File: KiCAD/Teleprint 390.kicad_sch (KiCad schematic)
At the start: 0 parts

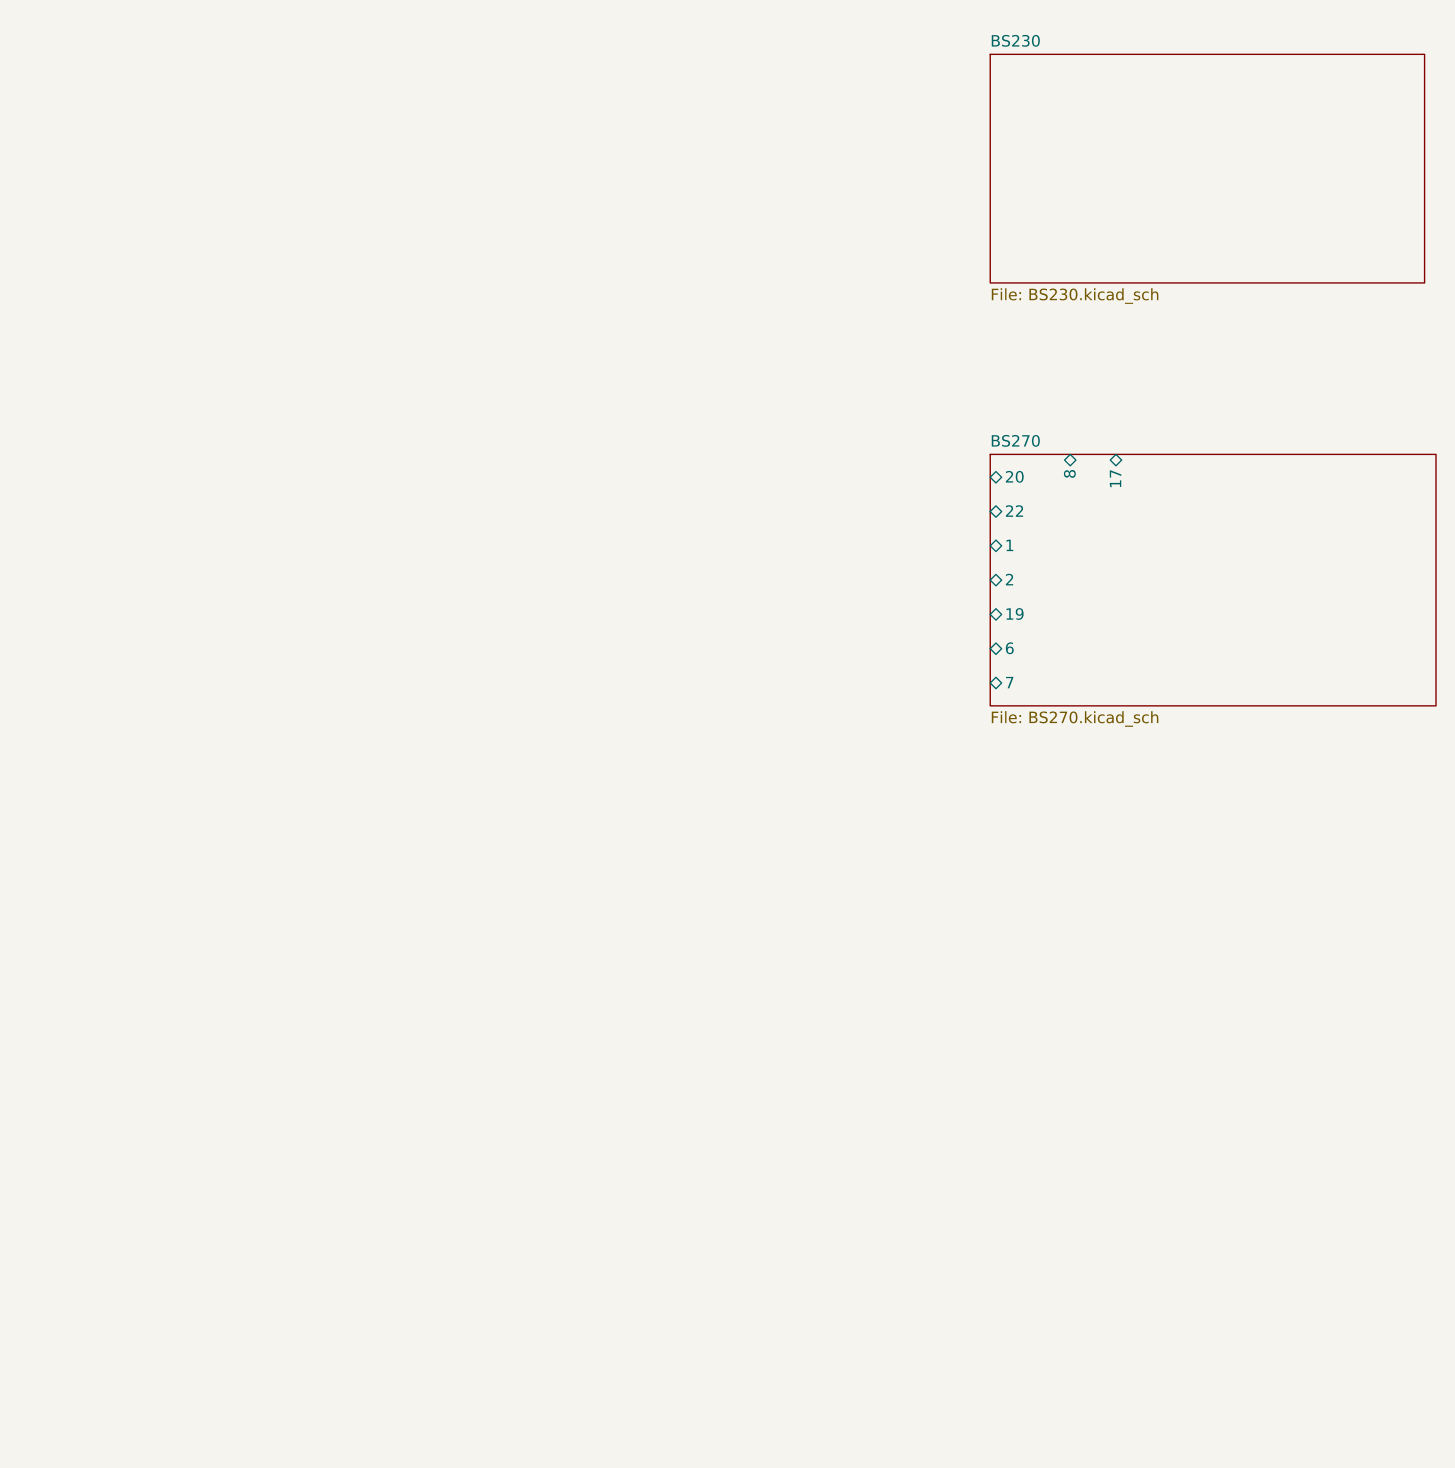
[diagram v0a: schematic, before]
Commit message: Schematics for BS112, BS230 and BS263 added
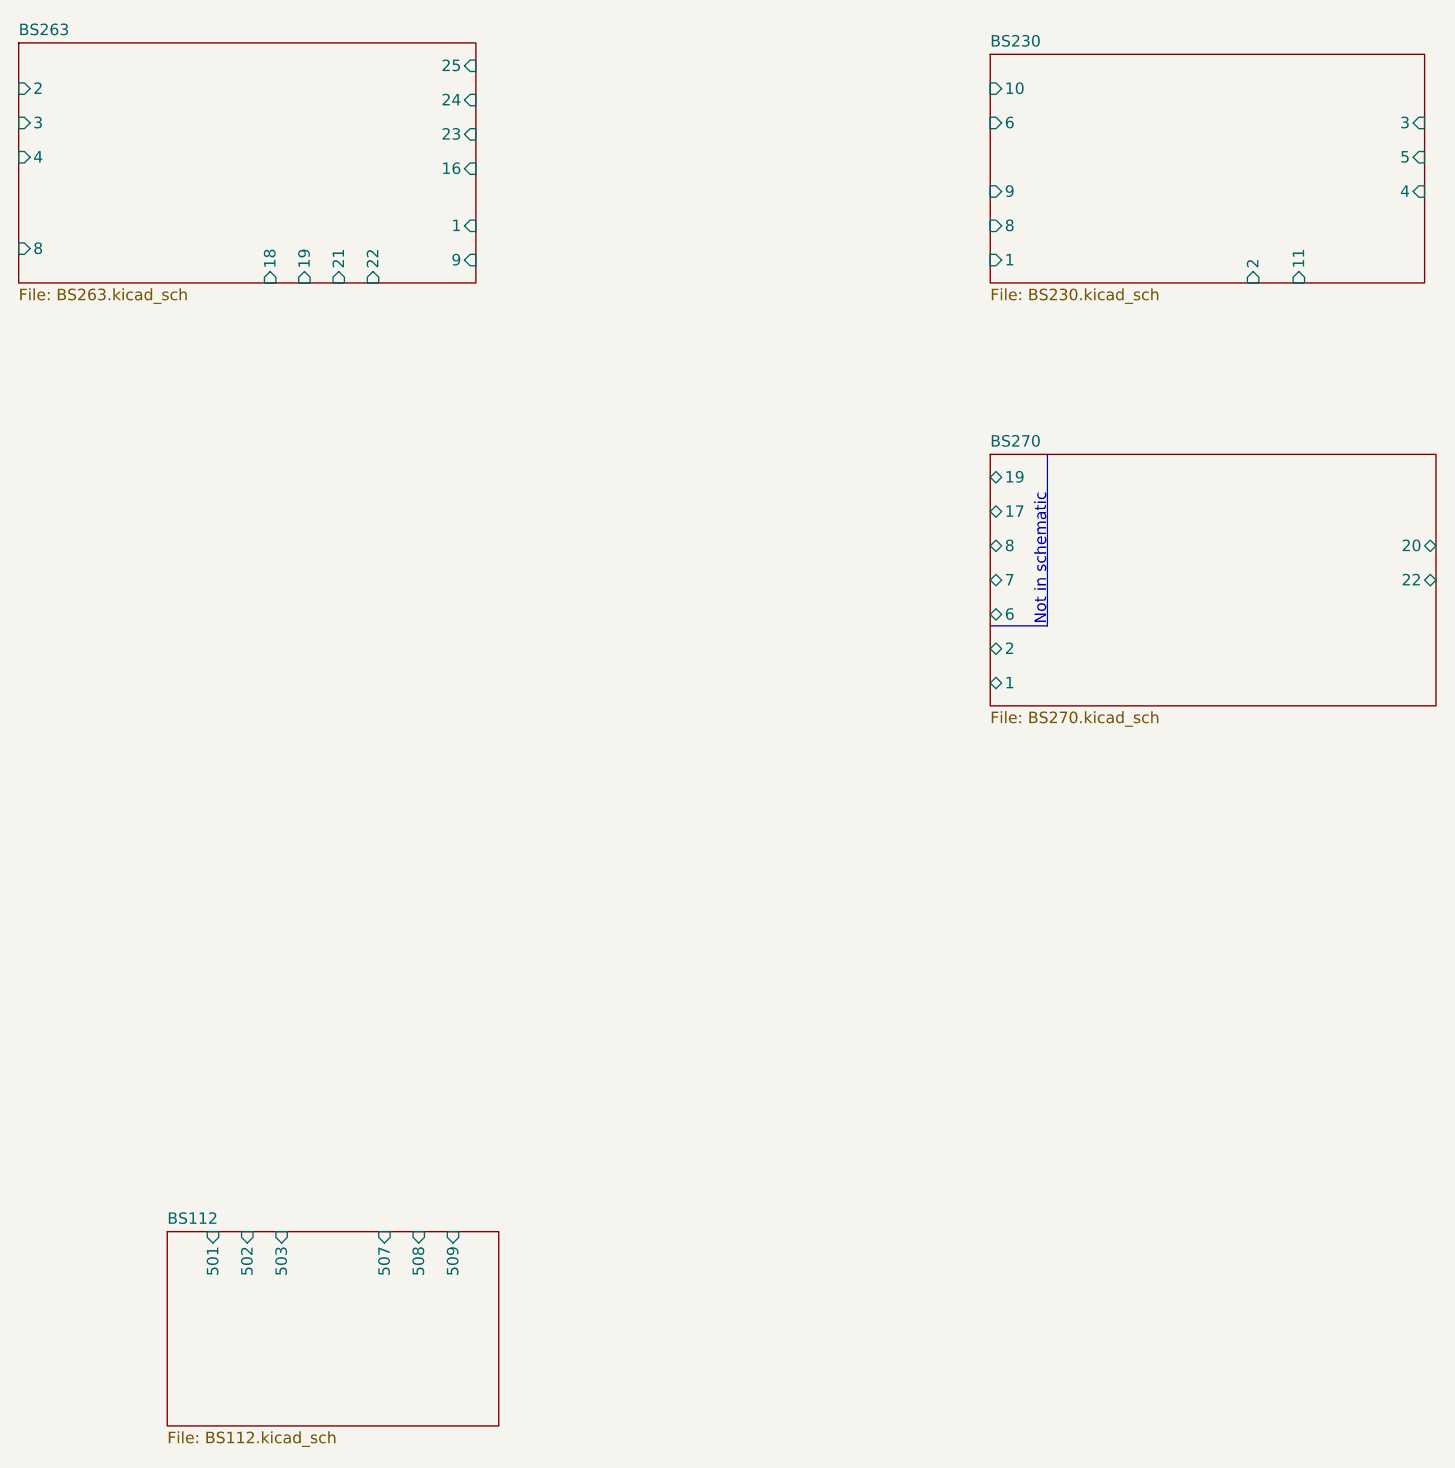
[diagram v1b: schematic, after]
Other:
- added sheet BS112 (BS112.kicad_sch)
- added sheet BS263 (BS263.kicad_sch)
- sheet BS230 ports: added 1, 10, 11, 2, 3, 4, 5, 6, 8, 9; removed none
- note added: "Not in schematic"

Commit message: Connections finished
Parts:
- added C1: (no value), symbol Device:C_Small
- added J4: (no value), symbol Connector:Conn_01x15_Male
- added J5, J6, J7, J8: Conn_01x15_Male, symbol Connector:Conn_01x15_Male
- added J?: (no value), symbol Connector:Conn_01x04_Female
- added J?: (no value), symbol Connector:Conn_01x12_Male
- added R1: (no value), symbol Device:R_Small
- added SW? (x7): (no value), symbol Switch:SW_DPDT_x2
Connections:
- new net: J?.1 (Pin_1), SW?.2 (B)
- new net: J?.2 (Pin_2), SW?.1 (A), SW?.3 (C)
- new net: J6.1 (Pin_1), J7.1 (Pin_1), J8.1 (Pin_1), J?.3 (Pin_3), R1.2, SW?.1 (A), SW?.1 (A)
- new net: J?.4 (Pin_4), SW?.2 (B)
- new net: J7.10 (Pin_10), J8.10 (Pin_10)
- new net: J4.14 (Pin_14), J7.14 (Pin_14)
- new net: J6.2 (Pin_2), J7.2 (Pin_2), J8.2 (Pin_2)
- new net: J6.3 (Pin_3), J7.3 (Pin_3), J8.3 (Pin_3)
- new net: J6.4 (Pin_4), J7.4 (Pin_4), J8.4 (Pin_4)
- new net: J6.5 (Pin_5), J7.5 (Pin_5), J8.5 (Pin_5)
- new net: J6.6 (Pin_6), J7.6 (Pin_6), J8.6 (Pin_6)
- new net: J6.7 (Pin_7), J7.7 (Pin_7), J8.7 (Pin_7)
- new net: J6.8 (Pin_8), J7.8 (Pin_8), J8.8 (Pin_8)
- new net: J6.9 (Pin_9), J7.9 (Pin_9), J8.9 (Pin_9)
- new net: J6.11 (Pin_11), J?.10 (Pin_10)
- new net: J4.6 (Pin_6), J6.12 (Pin_12)
- new net: J4.4 (Pin_4), J6.13 (Pin_13)
- new net: J4.11 (Pin_11), J4.15 (Pin_15), J4.8 (Pin_8), J8.12 (Pin_12)
- new net: J4.3 (Pin_3), J?.9 (Pin_9)
- new net: C1.2, R1.1
- new net: J8.13 (Pin_13), J8.14 (Pin_14)
- new net BS112/501 SWB Motor: J5.1 (Pin_1)
- new net BS112/502 SWA Motor: J5.2 (Pin_2)
- new net BS112/503 SWB Motor: J5.3 (Pin_3)
- new net BS112/507 Com: J4.13 (Pin_13), J5.7 (Pin_7), J6.15 (Pin_15), J7.15 (Pin_15), J?.3 (Pin_3), SW?.2 (B)
- new net BS112/508 LA Netz: J5.8 (Pin_8), J?.5 (Pin_5)
- new net BS112/509 LA Motor: J5.9 (Pin_9)
- new net BS230 D/10 +24V: J4.10 (Pin_10), J4.5 (Pin_5), J7.13 (Pin_13), J8.15 (Pin_15)
- new net BS230 D/11 Sel Mag: J4.9 (Pin_9)
- new net BS230 D/3 9VAC: J?.4 (Pin_4)
- new net BS230 D/4 9VAC: J?.2 (Pin_2)
- new net BS230 D/8 Tx Distr: SW?.1 (A), SW?.3 (C)
- new net BS263 C/21 K2B: J4.1 (Pin_1), J6.10 (Pin_10), SW?.6 (C)
- new net BS263 C/22 K2A: J?.12 (Pin_12), SW?.5 (B)
- new net BS263 C/24 18VAC: J?.1 (Pin_1)
- new net BS270 A/1 0V: J?.7 (Pin_7), SW?.2 (B)
- new net BS270 A/2 TX Distr Scan: C1.1, J7.11 (Pin_11), SW?.3 (C)
- new net BS270 A/20 64VAC: J?.6 (Pin_6)
- new net BS270 A/22 64VAC: J?.8 (Pin_8)
- new net BS270 A/7 KB: J6.14 (Pin_14), SW?.4 (A)
- new net BS270 A/8 KA: J4.12 (Pin_12), SW?.5 (B)
- new net Earth_Protective: J?.11 (Pin_11)
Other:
- sheet BS230 renamed BS230 D
- sheet BS263 renamed BS263 C
- sheet BS270 renamed BS270 A
- sheet BS112 ports: added 501 SWB Motor, 502 SWA Motor, 503 SWB Motor, 507 Com, 508 LA Netz, 509 LA Motor; removed 501, 502, 503, 507, 508, 509
- sheet BS230 D ports: added 1 -10V, 10 +24V, 11 Sel Mag, 2 Auto Start, 3 9VAC, 4 9VAC, 5 0V, 6 +10V, 8 Tx Distr, 9 TX Distr Scan; removed 1, 10, 11, 2, 3, 4, 5, 6, 8, 9
- sheet BS263 C ports: added 1 0V, 16 +10V, 18 K1B, 19 K1A, 2 Start Btn, 21 K2B, 22 K2A, 23 18VAC, 24 18VAC, 25 +24V, 3 Auto Start, 8 -10V; removed 1, 16, 18, 19, 2, 21, 22, 23, 24, 25, 3, 8
- sheet BS270 A ports: added 1 0V, 17 K, 19 K, 2 TX Distr Scan, 20 64VAC, 22 64VAC, 6 K, 7 KB, 8 KA; removed 1, 17, 19, 2, 20, 22, 6, 7, 8
- note added: "A"
- note added: "Add. wire"
- note added: "B"
- note added: "C"
- note added: "D"
- note added: "Distributor / Answerback"
- note added: "E"
- note added: "F"
- note added: "G"
- note added: "Keyboard"
- note added: "Local Line"
- note added: "Motor"
- note added: "Reader"
- note added: "RxD+"
- note added: "RxD-"
- note added: "Switch Assembly"
- note added: "TxD+"
- note added: "TxD-"

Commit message: Labels
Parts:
- added SW?: (no value), symbol Switch:SW_SPST
- C1: value (none) -> 100n
- J4: value (none) -> Conn_01x15_Male
- J?: value (none) -> Conn_01x04_Female
- J?: value (none) -> Conn_01x12_Male
- R1: value (none) -> 100
- SW? (x7): value (none) -> SW_DPDT_x2
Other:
- note added: "0V"
- note added: "1"
- note added: "115V"
- note added: "18V"
- note added: "2"
- note added: "3"
- note added: "4"
- note added: "5"
- note added: "6"
- note added: "64V"
- note added: "7"
- note added: "8"
- note added: "9V"
- note added: "Common"
- note added: "Rotor"

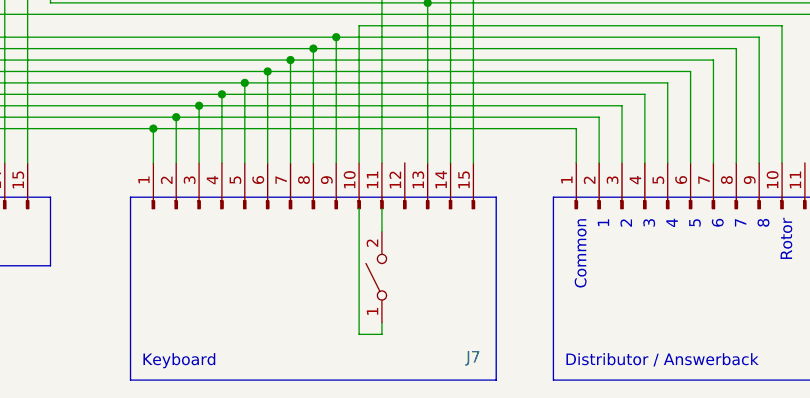
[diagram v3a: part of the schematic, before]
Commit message: Break Key added
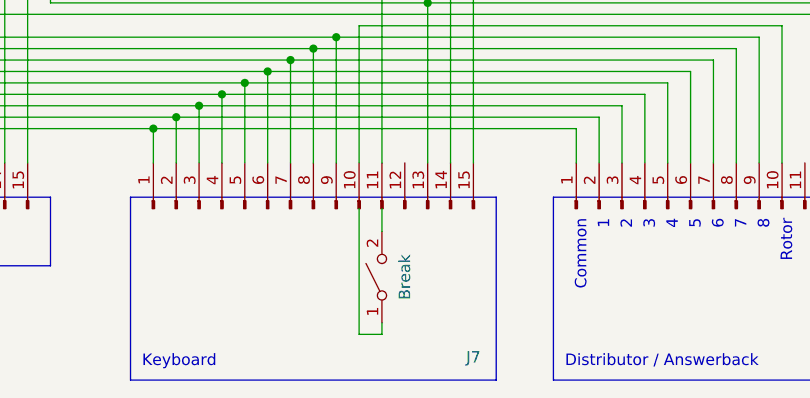
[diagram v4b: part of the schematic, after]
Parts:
- SW?: value (none) -> Break
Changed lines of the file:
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@@
       (effects (font (size 1.27 1.27)) (justify right) hide)
     )
-    (property "Value" "" (id 1) (at 288.29 229.87 0)
+    (property "Value" "Break" (id 1) (at 288.29 229.87 0)
       (effects (font (size 1.27 1.27)) (justify right))
     )
@@
       (reference "D3") (unit 1) (value "ZS70") (footprint "")
     )
+    (path "/9fbb2cdd-34c8-463e-9182-0816f704241f/00000000-0000-0000-0000-0000625584c8"
+      (reference "D4") (unit 1) (value "ZS70") (footprint "")
+    )
     (path "/101b9162-4dd2-4598-8eb9-9b7e9c3ad37f/00000000-0000-0000-0000-0000625584c8"
       (reference "D4") (unit 1) (value "ZS70") (footprint "")
     )
-    (path "/9fbb2cdd-34c8-463e-9182-0816f704241f/00000000-0000-0000-0000-0000625584c8"
-      (reference "D4") (unit 1) (value "ZS70") (footprint "")
-    )
     (path "/9fbb2cdd-34c8-463e-9182-0816f704241f/00000000-0000-0000-0000-0000625564d1"
       (reference "D5") (unit 1) (value "ZS70") (footprint "")
@@
       (reference "D?") (unit 1) (value "1N4007") (footprint "Diode_THT:D_DO-41_SOD81_P10.16mm_Horizontal")
     )
+    (path "/9fbb2cdd-34c8-463e-9182-0816f704241f/00000000-0000-0000-0000-00006255a945"
+      (reference "F1") (unit 1) (value "1.5A") (footprint "")
+    )
     (path "/101b9162-4dd2-4598-8eb9-9b7e9c3ad37f/00000000-0000-0000-0000-00006255a945"
       (reference "F1") (unit 1) (value "1.5A") (footprint "")
     )
-    (path "/9fbb2cdd-34c8-463e-9182-0816f704241f/00000000-0000-0000-0000-00006255a945"
-      (reference "F1") (unit 1) (value "1.5A") (footprint "")
-    )

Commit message: Labels added
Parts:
- added SW?: (no value), symbol Switch:SW_Push_Open
- SW?: symbol Switch:SW_SPST -> Switch:SW_Push_Open
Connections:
- net 115VAC: now reaches J4.3 (Pin_3), J?.9 (Pin_9)
- net BS230 D/10 +24V renamed +24V
- net BS263 C/21 K2B renamed 115VAC Sw
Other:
- note added: "Distr Trip Mag"
- note added: "NC"
- note added: "Supply"

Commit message: BS240 added
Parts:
- added D?: (no value), symbol Diode:1N4001
- added D?: 1N4001, Diode_THT:D_DO-41_SOD81_P10.16mm_Horizontal, symbol Diode:1N4001
- added SW?: (no value), symbol Switch:SW_Push
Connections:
- net BS270 A/8 KA is gone; now on net BS270 A/7 KB: J4.12 (Pin_12), SW?.5 (B)
- net +24V: now also J4.11 (Pin_11), J4.15 (Pin_15), J4.8 (Pin_8), J8.12 (Pin_12), D?.1 (K), D?.2 (A)
- net BS270 A/7 KB: now also D?.2 (A)
- net at J4.14 (Pin_14), J7.14 (Pin_14): now also D?.1 (K)
- net BS112/501 SWB Motor renamed +10V
- net BS112/507 Com renamed 0V
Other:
- added sheet BS240 B (BS240.kicad_sch)
- note added: "105V"
- note added: "105VAC"
- note added: "12,13?"
- note added: "14,15?"
- note added: "Local Power Supply"
- note added: "Motor Control"
- note added: "Selector Mag"
- note added: "Selector Magnet Driver"
- note added: "Tape Reader Power"
- note removed: "Supply"
